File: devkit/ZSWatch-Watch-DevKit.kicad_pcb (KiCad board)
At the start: 4 copper layers, 100 x 70 mm, 129 parts, among them IC401 nPM1300-QEXX, IC501 APDS-9306-065, IC502 BMI270, IC503 LIS2MDLTR, IC504 BMP581, IC505 DRV2603RUNT, IC506 PCA9306JK, IC507 RV-8263-C8, IC601 FAN5622SX, IC602 USBLC6-2P6, IC603 MX25U51245GZ4I00, IC604 NTS0104GU12, M601 NORA-B106, Q401 PMZ550UNEYL, Q402 PMZ550UNEYL, Q403 PMZ550UNEYL, Q404 PMZB320UPEYL, X401 Battery, X402 Battery, X403 Power, X501 Current, X502 I2S, X503 Current, X504 I2C, X505 Current, X506 Current, X507 Current, X508 Current, X509 Motor, X510 Current, X601 DEBUG, X602 Current, X603 Device, X604 UART, X605 GPIO, X606 Current, X607 IO Current, X608 Display, X609 Touch Current, X610 LED Current

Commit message: Revert "Bug: Issue #172"
This reverts commit d2b21792fba04b32ee89f1631bab4de80096e44a.
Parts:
- R503: value 200k -> 100k
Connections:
- IC506 pad 7: Net-(IC506-EN) -> /Project Architecture/Peripherals/VBAT
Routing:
- net /Project Architecture/Peripherals/VBAT: track 22.1 -> 23.0 mm, vias 5 -> 6
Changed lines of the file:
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@@
 			(size 0.65 0.17)
 			(layers "F.Cu" "F.Mask" "F.Paste")
-			(net 147 "Net-(IC506-EN)")
+			(net 5 "/Project Architecture/Peripherals/VBAT")
 			(pinfunction "VCC_{2}")
 			(pintype "power_in")
@@
 			)
 		)
-		(property "Value" "200k"
+		(property "Value" "100k"
 			(at 0 1.17 0)
 			(layer "F.Fab")
@@
 			)
 		)
-		(property "manf#" "RC0402FR-07200KL"
+		(property "manf#" "RC0402FR-07100KL"
 			(at 0 0 0)
 			(unlocked yes)
@@
 			)
 		)
-		(property "mouser#" "603-RC0402FR-07200KL"
+		(property "mouser#" "603-RC0402FR-07100KL"
 			(at 0 0 0)
 			(unlocked yes)
@@
 	)
 	(segment
+		(start 209.875 174.15)
+		(end 209.35 174.15)
+		(width 0.2)
+		(layer "F.Cu")
+		(net 5)
+	)
+	(segment
 		(start 227.8 117.5)
 		(end 226.8 116.5)
@@
 	)
 	(segment
+		(start 209.35 174.15)
+		(end 209.1 174.4)
+		(width 0.2)
+		(layer "F.Cu")
+		(net 5)
+	)
+	(segment
 		(start 203.87 177.23)
 		(end 203.9 177.2)
@@
 	)
 	(via
+		(at 209.1 174.4)
+		(size 0.45)
+		(drill 0.25)
+		(layers "F.Cu" "B.Cu")
+		(net 5)
+	)
+	(via
 		(at 228.4 119.8)
 		(size 0.45)
@@
 		(end 209.875 174.5)
 		(width 0.2)
-		(layer "F.Cu")
-		(net 147)
-	)
-	(segment
-		(start 209.875 174.15)
-		(end 209.875 174.5)
-		(width 0.2)

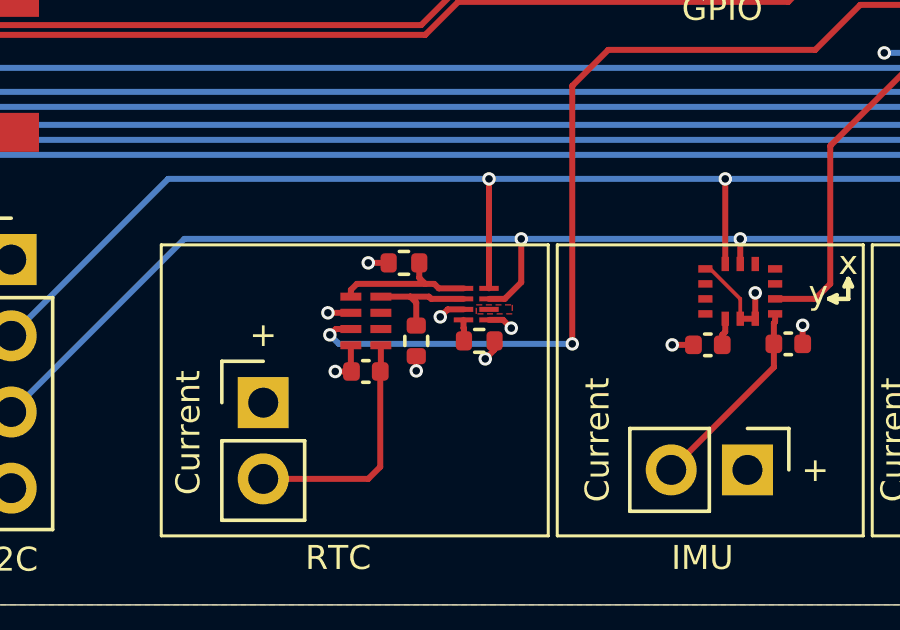
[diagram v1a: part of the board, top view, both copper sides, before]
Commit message: Bug: Issue #172
- Fix wrong resistor for VREF2 pin for the level shifter
- Update changelog

Closes #172

Signed-off-by: Daniel Kampert <DanielKampert@kampis-elektroecke.de>
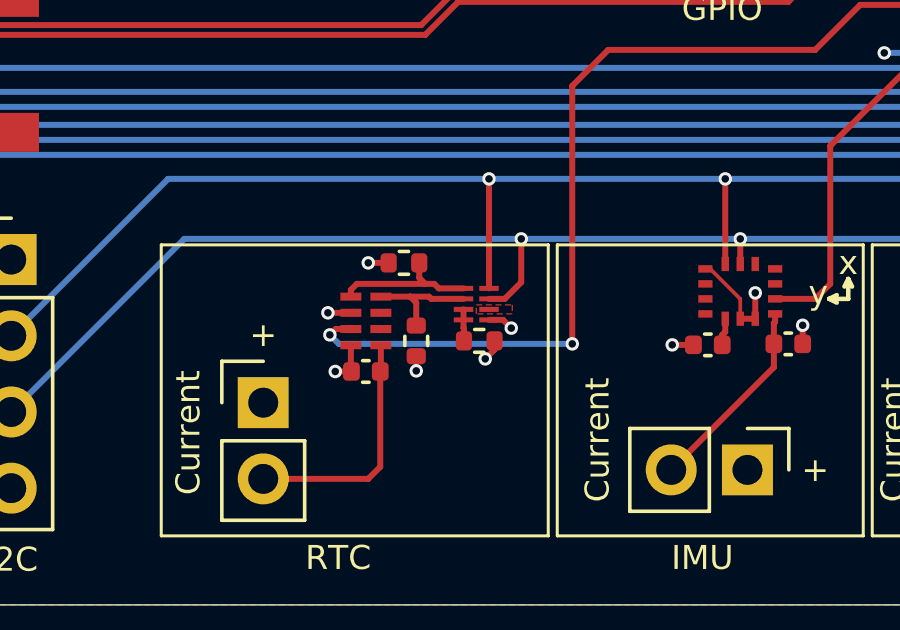
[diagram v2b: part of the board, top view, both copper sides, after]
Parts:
- R503: value 100k -> 200k
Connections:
- IC506 pad 7: /Project Architecture/Peripherals/VBAT -> Net-(IC506-EN)
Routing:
- net /Project Architecture/Peripherals/VBAT: track 23.0 -> 22.1 mm, vias 6 -> 5
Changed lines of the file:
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@@
 			(size 0.65 0.17)
 			(layers "F.Cu" "F.Mask" "F.Paste")
-			(net 5 "/Project Architecture/Peripherals/VBAT")
+			(net 147 "Net-(IC506-EN)")
 			(pinfunction "VCC_{2}")
 			(pintype "power_in")
@@
 			)
 		)
-		(property "Value" "100k"
+		(property "Value" "200k"
 			(at 0 1.17 0)
 			(layer "F.Fab")
@@
 			)
 		)
-		(property "manf#" "RC0402FR-07100KL"
+		(property "manf#" "RC0402FR-07200KL"
 			(at 0 0 0)
 			(unlocked yes)
@@
 			)
 		)
-		(property "mouser#" "603-RC0402FR-07100KL"
+		(property "mouser#" "603-RC0402FR-07200KL"
 			(at 0 0 0)
 			(unlocked yes)
@@
 	)
 	(segment
-		(start 209.875 174.15)
-		(end 209.35 174.15)
-		(width 0.2)
-		(layer "F.Cu")
-		(net 5)
-	)
-	(segment
 		(start 227.8 117.5)
 		(end 226.8 116.5)
@@
 	)
 	(segment
-		(start 209.35 174.15)
-		(end 209.1 174.4)
-		(width 0.2)
-		(layer "F.Cu")
-		(net 5)
-	)
-	(segment
 		(start 203.87 177.23)
 		(end 203.9 177.2)
@@
 	)
 	(via
-		(at 209.1 174.4)
-		(size 0.45)
-		(drill 0.25)
-		(layers "F.Cu" "B.Cu")
-		(net 5)
-	)
-	(via
 		(at 228.4 119.8)
 		(size 0.45)
@@
 		(end 209.875 174.5)
 		(width 0.2)
+		(layer "F.Cu")
+		(net 147)
+	)
+	(segment
+		(start 209.875 174.15)
+		(end 209.875 174.5)
+		(width 0.2)

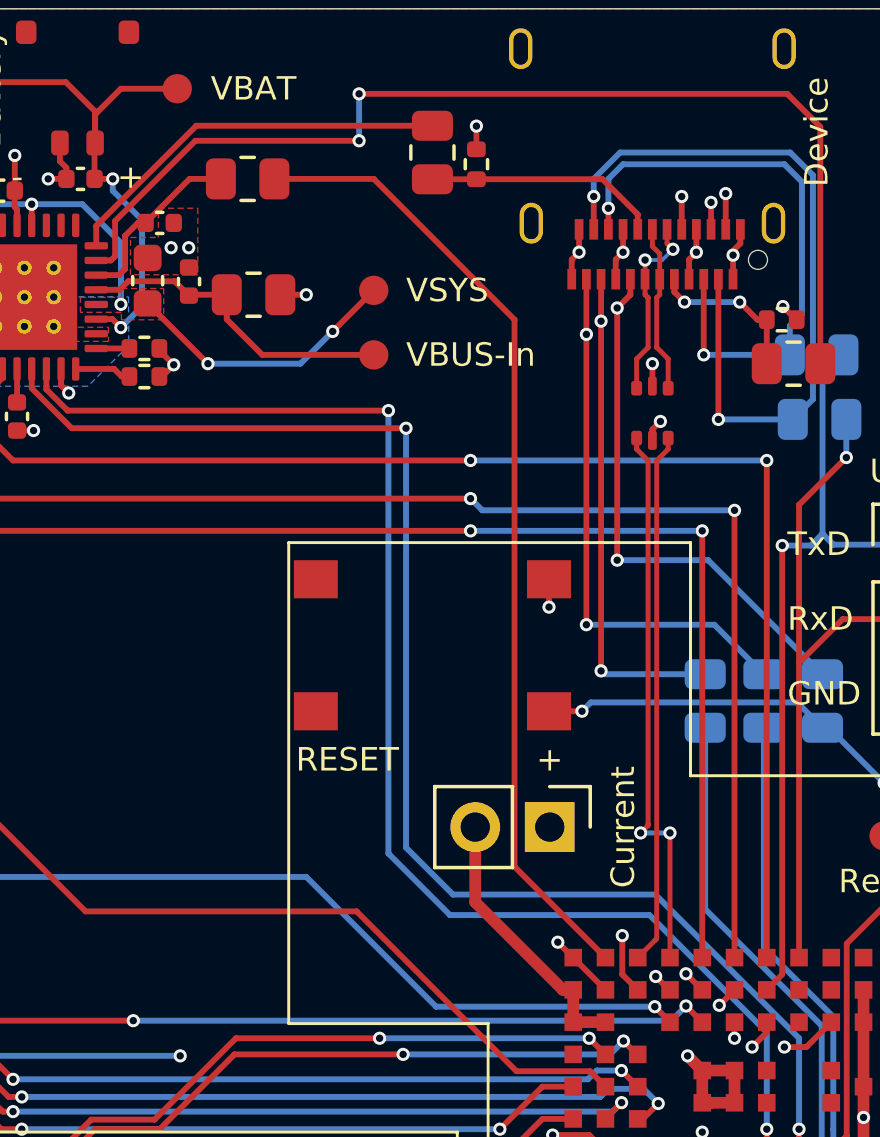
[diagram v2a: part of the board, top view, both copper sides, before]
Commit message: Feature: Issue #174
Add allignment markers for the MCU module to the copper layer

Closes #174

Signed-off-by: Daniel Kampert <DanielKampert@kampis-elektroecke.de>
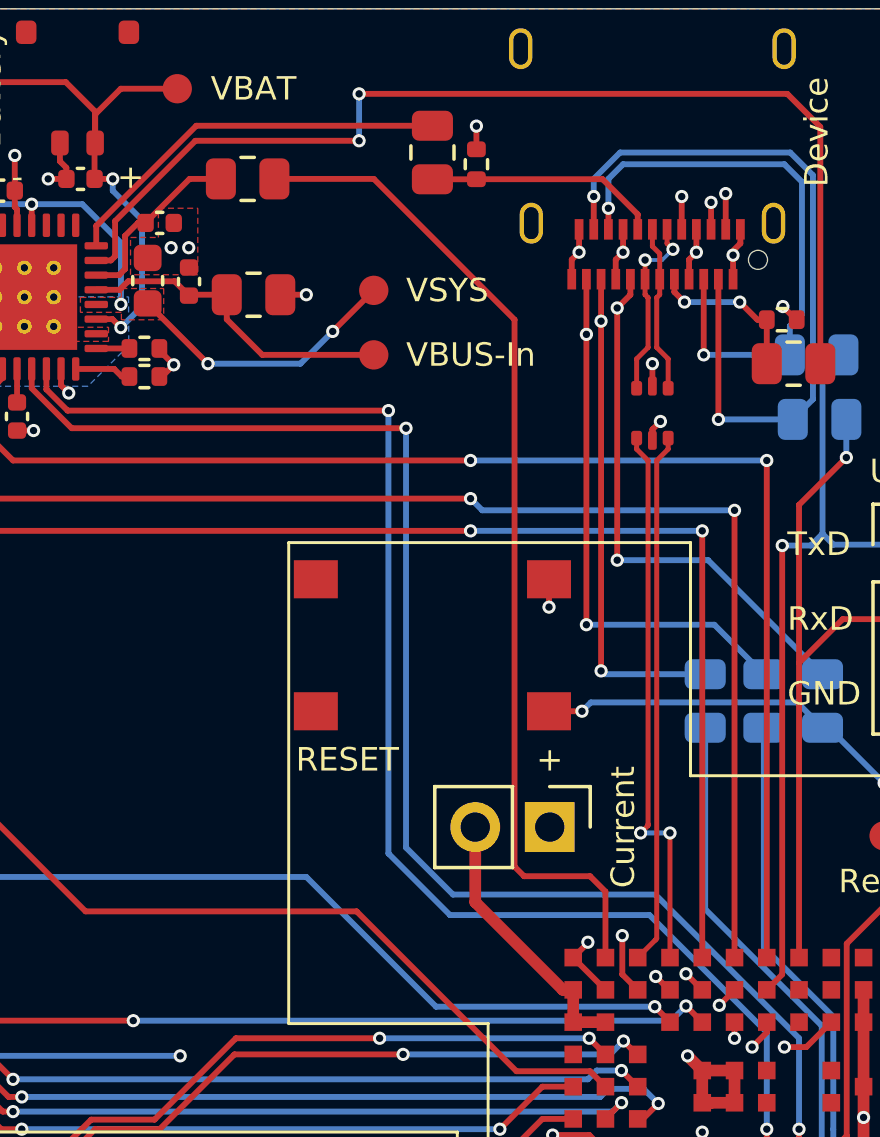
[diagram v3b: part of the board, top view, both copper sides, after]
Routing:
- net /Project Architecture/MCU/USB-VBUS-Out: track 33.2 -> 34.5 mm
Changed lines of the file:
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@@
 		)
 	)
+	(gr_poly
+		(pts
+			(xy 243.2 145.02092) (xy 242.8 145.42092) (xy 243.2 145.42092)
+		)
+		(stroke
+			(width 0.1)
+			(type solid)
+		)
+		(fill yes)
+		(layers "F.Cu" "F.Mask")
+	)
+	(gr_poly
+		(pts
+			(xy 242.8 156.07092) (xy 243.2 156.47092) (xy 243.2 156.07092)
+		)
+		(stroke
+			(width 0.1)
+			(type solid)
+		)
+		(fill yes)
+		(layers "F.Cu" "F.Mask")
+	)
 	(gr_rect
 		(start 172.1 116.2)
@@
 	)
 	(segment
+		(start 244.6 145.85)
+		(end 244.1 146.35)
+		(width 0.2)
+		(layer "F.Cu")
+		(net 1)
+	)
+	(segment
 		(start 170.61 141.1)
 		(end 170.61 140.7)
@@
 	)
 	(segment
-		(start 243.575 145.825)
-		(end 244.1 146.35)
-		(width 0.2)
-		(layer "F.Cu")
-		(net 1)
-	)
-	(segment
 		(start 236.62 175.4)
 		(end 236.62 174.775)
@@
 	)
 	(segment
+		(start 244.6 145.825)
+		(end 244.6 145.85)
+		(width 0.2)
+		(layer "F.Cu")
+		(net 1)
+	)
+	(segment
 		(start 201.99 145.1375)
 		(end 201.4 145.1375)
@@
 	)
 	(via
-		(at 243.575 145.825)
+		(at 244.6 145.825)
 		(size 0.45)
 		(drill 0.25)
@@
 	)
 	(segment
-		(start 237.3 119.8)
-		(end 242.1 124.6)
+		(start 242.1 124.6)
+		(end 237.3 119.8)
 		(width 0.2)
 		(layer "F.Cu")
@@
 	(segment
 		(start 242.1 143.25)
-		(end 245.2 146.35)
+		(end 242.1 124.6)
 		(width 0.2)
 		(layer "F.Cu")
@@
 	)
 	(segment
-		(start 242.1 124.6)
-		(end 242.1 143.25)
+		(start 245.2 146.35)
+		(end 245.2 144.1)
 		(width 0.2)
 		(layer "F.Cu")
@@
 	)
 	(segment
-		(start 233.9125 119.8)
-		(end 237.3 119.8)
+		(start 244.675 143.575)
+		(end 242.425 143.575)
+		(width 0.2)
+		(layer "F.Cu")
+		(net 52)
+	)
+	(segment
+		(start 245.2 144.1)
+		(end 244.675 143.575)
+		(width 0.2)
+		(layer "F.Cu")
+		(net 52)
+	)
+	(segment
+		(start 237.3 119.8)
+		(end 233.9125 119.8)
+		(width 0.2)
+		(layer "F.Cu")
+		(net 52)
+	)
+	(segment
+		(start 242.425 143.575)
+		(end 242.1 143.25)
 		(width 0.2)
 		(layer "F.Cu")

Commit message: Revert "Feature: Issue #174"
This reverts commit a258055a47c56b8763088da3e06577d57b5d3abc.
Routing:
- net /Project Architecture/MCU/USB-VBUS-Out: track 34.5 -> 33.2 mm
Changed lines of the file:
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@@
 		)
 	)
-	(gr_poly
-		(pts
-			(xy 243.2 145.02092) (xy 242.8 145.42092) (xy 243.2 145.42092)
-		)
-		(stroke
-			(width 0.1)
-			(type solid)
-		)
-		(fill yes)
-		(layers "F.Cu" "F.Mask")
-	)
-	(gr_poly
-		(pts
-			(xy 242.8 156.07092) (xy 243.2 156.47092) (xy 243.2 156.07092)
-		)
-		(stroke
-			(width 0.1)
-			(type solid)
-		)
-		(fill yes)
-		(layers "F.Cu" "F.Mask")
-	)
 	(gr_rect
 		(start 172.1 116.2)
@@
 	)
 	(segment
-		(start 244.6 145.85)
-		(end 244.1 146.35)
-		(width 0.2)
-		(layer "F.Cu")
-		(net 1)
-	)
-	(segment
 		(start 170.61 141.1)
 		(end 170.61 140.7)
@@
 	)
 	(segment
+		(start 243.575 145.825)
+		(end 244.1 146.35)
+		(width 0.2)
+		(layer "F.Cu")
+		(net 1)
+	)
+	(segment
 		(start 236.62 175.4)
 		(end 236.62 174.775)
@@
 	)
 	(segment
-		(start 244.6 145.825)
-		(end 244.6 145.85)
-		(width 0.2)
-		(layer "F.Cu")
-		(net 1)
-	)
-	(segment
 		(start 201.99 145.1375)
 		(end 201.4 145.1375)
@@
 	)
 	(via
-		(at 244.6 145.825)
+		(at 243.575 145.825)
 		(size 0.45)
 		(drill 0.25)
@@
 	)
 	(segment
-		(start 242.1 124.6)
-		(end 237.3 119.8)
-		(width 0.2)
-		(layer "F.Cu")
-		(net 52)
-	)
-	(segment
-		(start 242.1 143.25)
+		(start 237.3 119.8)
 		(end 242.1 124.6)
 		(width 0.2)
@@
 	)
 	(segment
-		(start 245.2 146.35)
-		(end 245.2 144.1)
-		(width 0.2)
-		(layer "F.Cu")
-		(net 52)
-	)
-	(segment
-		(start 244.675 143.575)
-		(end 242.425 143.575)
-		(width 0.2)
-		(layer "F.Cu")
-		(net 52)
-	)
-	(segment
-		(start 245.2 144.1)
-		(end 244.675 143.575)
+		(start 242.1 143.25)
+		(end 245.2 146.35)
 		(width 0.2)
 		(layer "F.Cu")
@@
 	)
 	(segment
-		(start 237.3 119.8)
-		(end 233.9125 119.8)
+		(start 242.1 124.6)
+		(end 242.1 143.25)
 		(width 0.2)
 		(layer "F.Cu")
@@
 	)
 	(segment
-		(start 242.425 143.575)
-		(end 242.1 143.25)
+		(start 233.9125 119.8)
+		(end 237.3 119.8)
 		(width 0.2)
 		(layer "F.Cu")
